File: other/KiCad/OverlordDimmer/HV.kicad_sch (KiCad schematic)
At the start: 23 parts, among them J1 1757310, J2 1757310, Q41 BC817, Q42 2SC4061KT146N, Q43 2SC4061KT146N

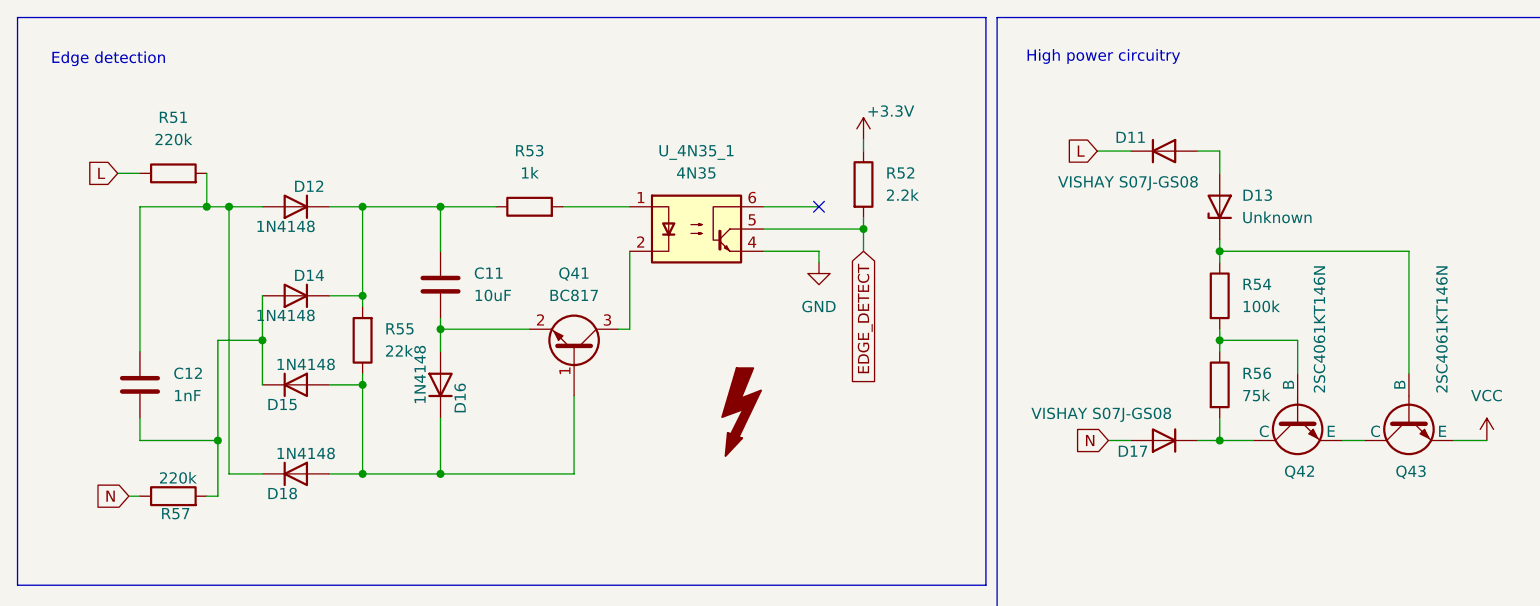
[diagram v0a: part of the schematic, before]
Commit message: sent to production
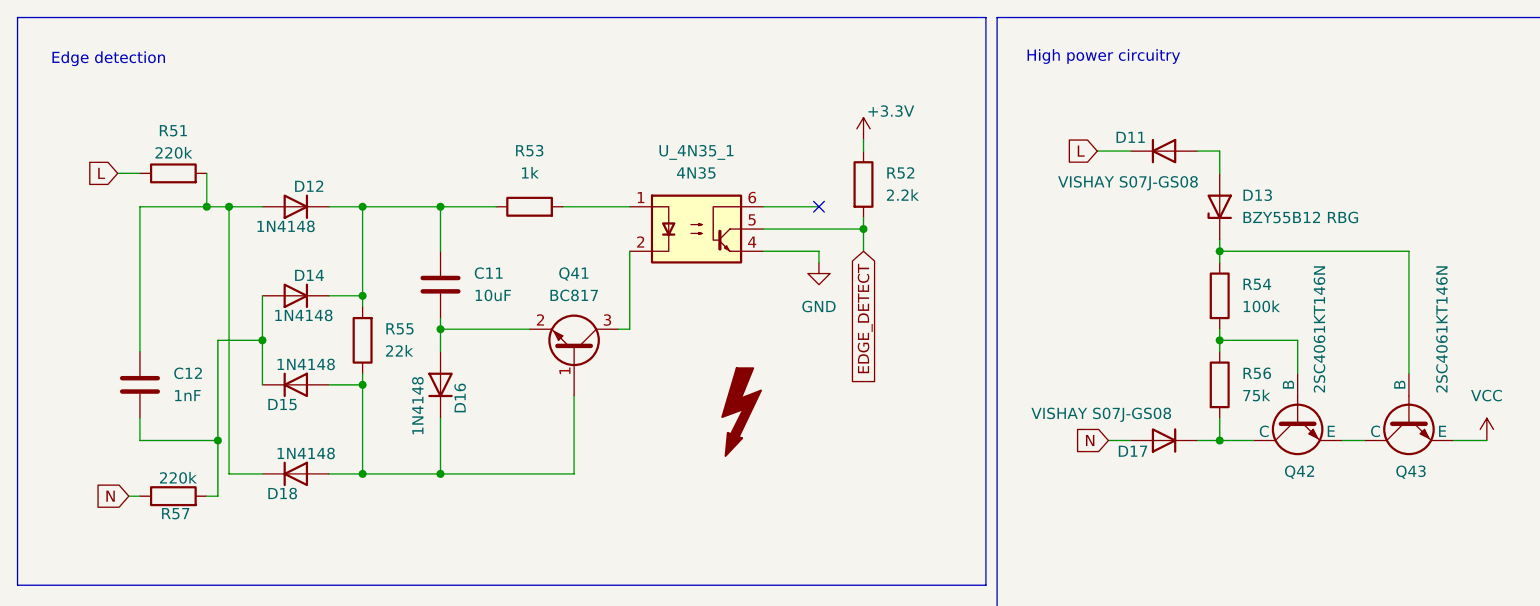
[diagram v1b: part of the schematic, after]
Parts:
- D13: value Unknown -> BZY55B12 RBG
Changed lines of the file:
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@@
-			)
-		)
-		(property "Sim.Enable" ""
-			(at 58.42 55.88 0)
-			(effects
-				(font
-					(size 1.27 1.27)
-				)
-				(hide yes)
 			)
 		)
@@
 			)
 		)
-		(property "Sim.Enable" ""
-			(at 156.21 60.96 0)
-			(effects
-				(font
-					(size 1.27 1.27)
-				)
-				(hide yes)
-			)
-		)
 		(pin "2"
 		)
@@
 			)
 		)
-		(property "Sim.Enable" ""
-			(at 50.8 71.12 0)
-			(effects
-				(font
-					(size 1.27 1.27)
-				)
-				(hide yes)
-			)
-		)
 		(pin "2"
 		)
@@
 		)
 		(property "Sim.Pins" "1=K 2=A"
-			(at 149.86 67.31 0)
-			(effects
-				(font
-					(size 1.27 1.27)
-				)
-				(hide yes)
-			)
-		)
-		(property "Sim.Enable" ""
 			(at 149.86 67.31 0)
 			(effects
@@
 			)
 		)
-		(property "Sim.Enable" ""
-			(at 50.8 60.96 0)
-			(effects
-				(font
-					(size 1.27 1.27)
-				)
-				(hide yes)
-			)
-		)
 		(pin "2"
 		)
@@
 			)
 		)
-		(property "Sim.Enable" ""
-			(at 82.55 57.15 0)
-			(effects
-				(font
-					(size 1.27 1.27)
-				)
-				(hide yes)
-			)
-		)
 		(pin "1"
 		)
@@
 			)
 		)
-		(property "Sim.Enable" ""
-			(at 96.52 43.18 0)
-			(effects
-				(font
-					(size 1.27 1.27)
-				)
-				(hide yes)
-			)
-		)
 		(pin "3"
 		)
@@
 			)
 		)
-		(property "Sim.Enable" ""
-			(at 115.57 38.1 0)
-			(effects
-				(font
-					(size 1.27 1.27)
-				)
-				(hide yes)
-			)
-		)
 		(pin "2"
 		)
@@
 			)
 		)
-		(property "Sim.Enable" ""
-			(at 156.21 50.8 0)
-			(effects
-				(font
-					(size 1.27 1.27)
-				)
-				(hide yes)
-			)
-		)
 		(pin "2"
 		)
@@
 			)
 		)
-		(property "Sim.Enable" ""
-			(at 149.86 34.29 0)
-			(effects
-				(font
-					(size 1.27 1.27)
-				)
-				(hide yes)
-			)
-		)
 		(pin "1"
 		)
@@
 		(on_board yes)
 		(dnp no)
-		(fields_autoplaced yes)
 		(property "Reference" "R51"
-			(at 36.83 30.48 90)
+			(at 36.83 32.004 90)
 			(effects
 				(font
@@
 		)
 		(property "Value" "220k"
-			(at 36.83 33.02 90)
+			(at 36.83 34.544 90)
 			(effects
 				(font
@@
 			)
 		)
-		(property "Sim.Enable" ""
-			(at 36.83 36.83 0)
-			(effects
-				(font
-					(size 1.27 1.27)
-				)
-				(hide yes)
-			)
-		)
 		(pin "1"
 		)
@@
 		)
 		(property "Description" ""
-			(at 36.83 73.66 0)
-			(effects
-				(font
-					(size 1.27 1.27)
-				)
-				(hide yes)
-			)
-		)
-		(property "Sim.Enable" ""
 			(at 36.83 73.66 0)
 			(effects
@@
 			)
 		)
-		(property "Sim.Enable" ""
-			(at 67.31 49.53 0)
-			(effects
-				(font
-					(size 1.27 1.27)
-				)
-				(hide yes)
-			)
-		)
 		(pin "2"
 		)
@@
 			)
 		)
-		(property "Value" "Unknown"
+		(property "Value" "BZY55B12 RBG"
 			(at 158.75 41.9099 90)
 			(effects
@@
 		)
 		(property "Description" "Zener diode"
-			(at 156.21 40.64 0)
-			(effects
-				(font
-					(size 1.27 1.27)
-				)
-				(hide yes)
-			)
-		)
-		(property "Sim.Enable" ""
 			(at 156.21 40.64 0)
 			(effects
@@
 			)
 		)
-		(property "Sim.Enable" ""
-			(at 177.8 64.77 0)
-			(effects
-				(font
-					(size 1.27 1.27)
-				)
-				(hide yes)
-			)
-		)
 		(pin "1"
 		)
@@
 		)
 		(property "Value" "1N4148"
-			(at 65.024 56.388 0)
+			(at 64.77 59.944 0)
 			(effects
 				(font
@@
 			)
 		)
-		(property "Sim.Enable" ""
-			(at 67.31 60.96 0)
-			(effects
-				(font
-					(size 1.27 1.27)
-				)
-				(hide yes)
-			)
-		)
 		(pin "2"
 		)
@@
 		)
 		(property "Sim.Pins" "1=K 2=A"
-			(at 50.8 40.64 0)
-			(effects
-				(font
-					(size 1.27 1.27)
-				)
-				(hide yes)
-			)
-		)
-		(property "Sim.Enable" ""
 			(at 50.8 40.64 0)
 			(effects
@@
 			)
 		)
-		(property "Sim.Enable" ""
-			(at 77.47 40.64 0)
-			(effects
-				(font
-					(size 1.27 1.27)
-				)
-				(hide yes)
-			)
-		)
 		(pin "1"
 		)
@@
 			)
 		)
-		(property "Sim.Enable" ""
-			(at 33.02 60.96 0)
-			(effects
-				(font
-					(size 1.27 1.27)
-				)
-				(hide yes)
-			)
-		)
 		(pin "2"
 		)
@@
 			)
 		)
-		(property "Sim.Enable" ""
-			(at 215.9 71.12 0)
-			(effects
-				(font
-					(size 1.27 1.27)
-				)
-				(hide yes)
-			)
-		)
 		(pin "1"
 		)
@@
 			)
 		)
-		(property "Sim.Enable" ""
-			(at 165.1 64.77 0)
-			(effects
-				(font
-					(size 1.27 1.27)
-				)
-				(hide yes)
-			)
-		)
 		(pin "1"
 		)
@@
 			)
 		)
-		(property "Sim.Enable" ""
-			(at 215.9 36.83 0)
-			(effects
-				(font
-					(size 1.27 1.27)
-				)
-				(hide yes)
-			)
-		)
 		(pin "1"
 		)
@@
 		)
 		(property "Value" "1N4148"
-			(at 46.228 53.086 0)
+			(at 48.26 53.086 0)
 			(effects
 				(font
@@
 			(at 50.8 50.8 0)
 			(effects
-				(font
-					(size 1.27 1.27)
-				)
-				(hide yes)
-			)
-		)
-		(property "Sim.Enable" ""
-			(at 50.8 50.8 0)
-			(effects

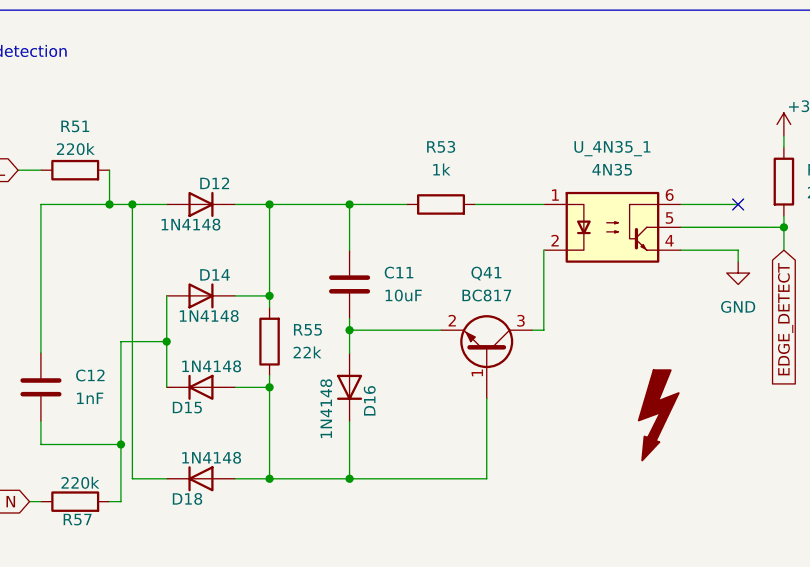
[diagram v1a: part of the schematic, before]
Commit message: update to latest rtdb_gen
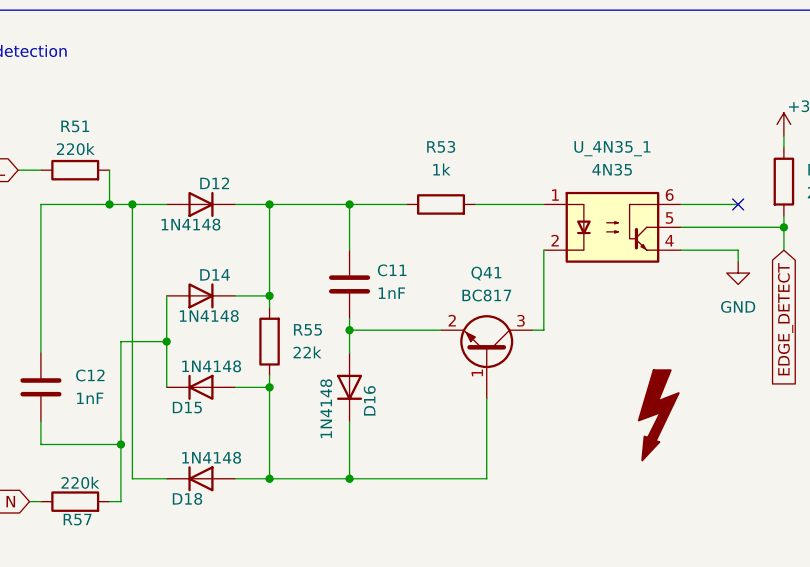
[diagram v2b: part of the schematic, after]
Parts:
- C11: value 10uF -> 1nF
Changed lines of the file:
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@@
 		(on_board yes)
 		(dnp no)
-		(fields_autoplaced yes)
 		(property "Reference" "C11"
-			(at 71.12 48.2599 0)
+			(at 70.358 48.006 0)
 			(effects
 				(font
@@
 			)
 		)
-		(property "Value" "10uF"
-			(at 71.12 50.7999 0)
+		(property "Value" "1nF"
+			(at 70.358 50.546 0)
 			(effects
 				(font

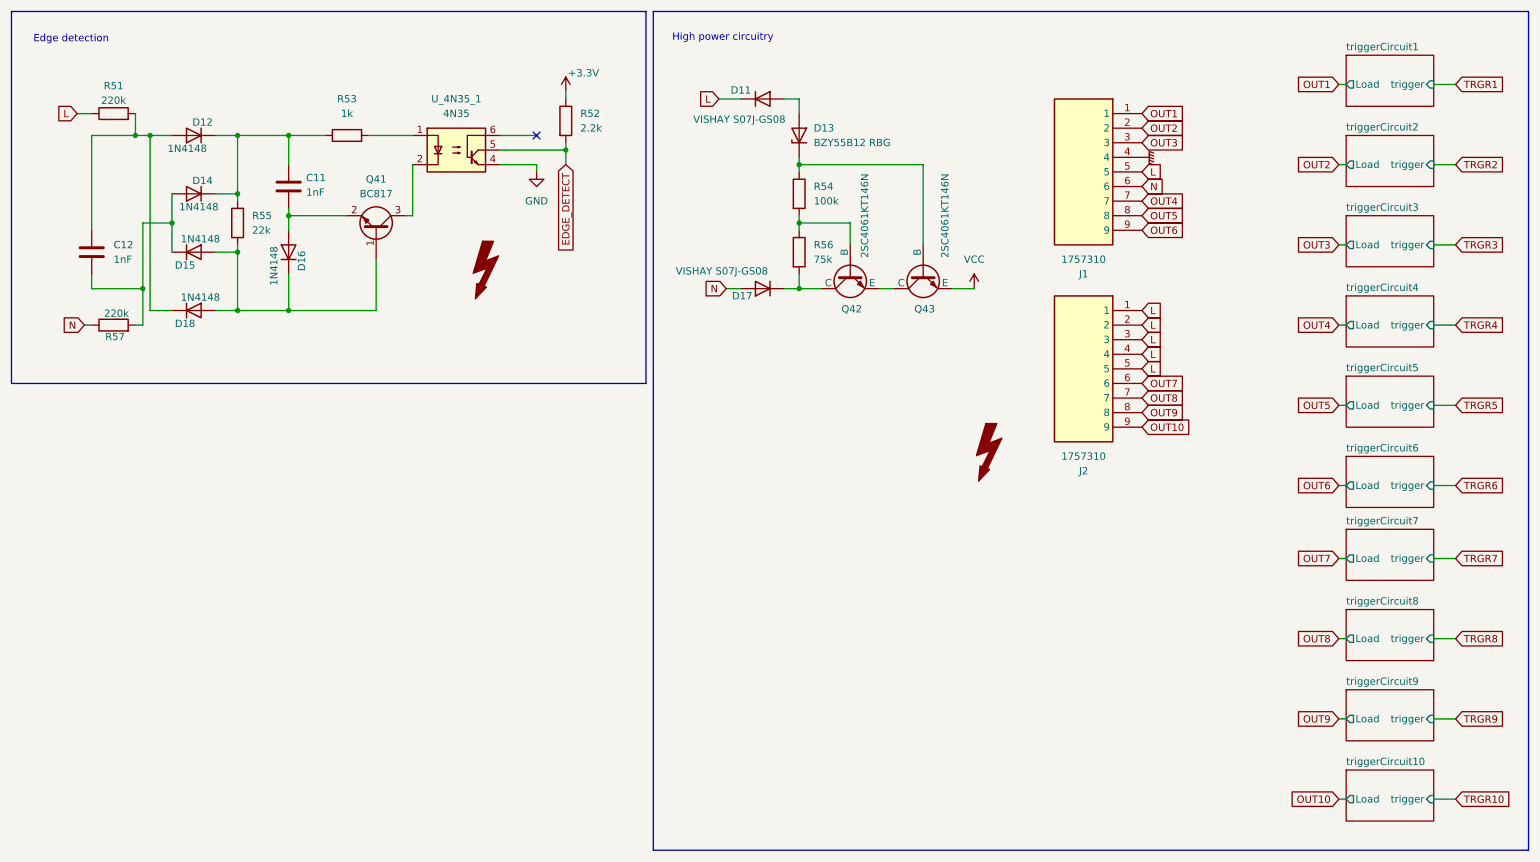
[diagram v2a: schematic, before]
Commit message: Sent for PCB production, ver 1.2 rev A
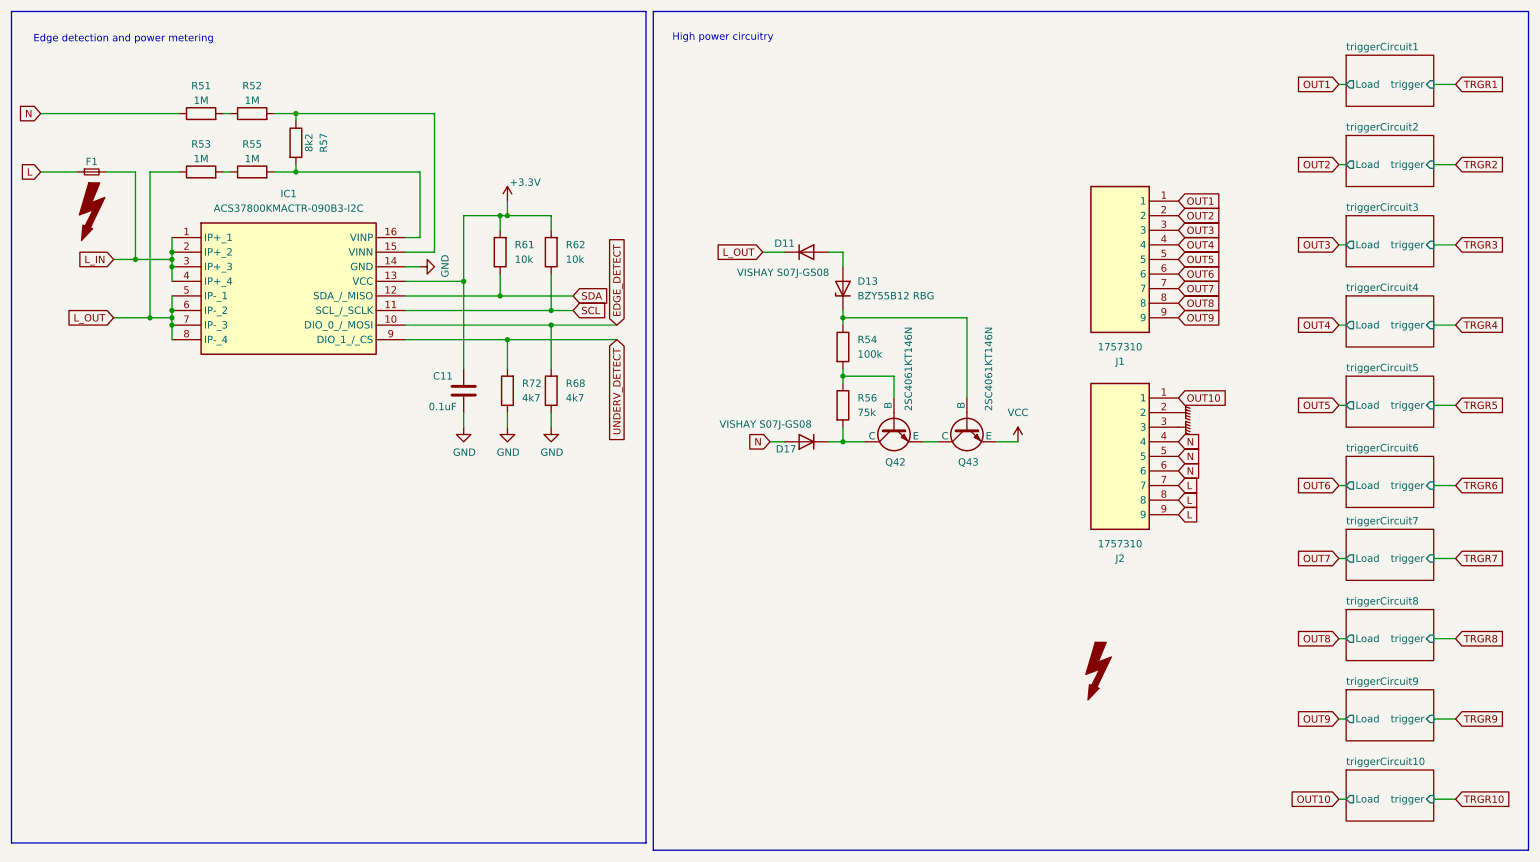
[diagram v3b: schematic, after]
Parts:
- removed C12: 1nF, Capacitor_SMD:C_0805_2012Metric_Pad1.18x1.45mm_HandSolder, symbol Device:C
- removed D12, D14, D15, D16, D18: 1N4148, Diode_SMD:D_0805_2012Metric_Pad1.15x1.40mm_HandSolder, symbol Diode:1N4148
- removed Q41: BC817, Package_TO_SOT_SMD:SOT-23, symbol Transistor_BJT:BC817
- removed U_4N35_1: 4N35, Package_DIP:DIP-6_W7.62mm, symbol Isolator:4N35
- added F1: Fuse_Small, Fuse:Fuseholder_Clip-5x20mm_Bel_FC-203-22_Lateral_P17.80x5.00mm_D1.17mm_Horizontal, symbol Device:Fuse_Small
- added IC1: ACS37800KMACTR-090B3-I2C, SOIC127P1030X265-16N, symbol ACS37800KMACTR-090B3-I2C:ACS37800KMACTR-090B3-I2C
- added R61, R62: 10k, Resistor_SMD:R_0805_2012Metric_Pad1.20x1.40mm_HandSolder, symbol Device:R
- added R68, R72: 4k7, Resistor_SMD:R_0805_2012Metric_Pad1.20x1.40mm_HandSolder, symbol Device:R
- C11: value 1nF -> 0.1uF
- R51: value 220k -> 1M
- R52: value 2.2k -> 1M
- R53: value 1k -> 1M
- R55: value 22k -> 1M
- R57: value 220k -> 8k2
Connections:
- net +3.3V: now also C11.1, IC1.13 (VCC), R61.2, R62.2; no longer R52.1
- net EDGE_DETECT: now also IC1.10 (DIO_0_/_MOSI), R68.2; no longer R52.2
- net GND: now also C11.2, IC1.14 (GND), R68.1, R72.1
- net GNDPWR: now also J2.2, J2.3; no longer J1.4
- net L: now also J2.7, J2.8, J2.9, F1.1; no longer D11.1 (K), J1.5, J2.1, J2.2, J2.3, J2.4, J2.5, R51.1
- net N: now also J2.4, J2.5, J2.6, R51.1; no longer J1.6, R57.1
- net OUT10: now also J2.1; no longer J2.9
- net OUT4: now also J1.4; no longer J1.7
- net OUT5: now also J1.5; no longer J1.8
- net OUT6: now also J1.6; no longer J1.9
- net OUT7: now also J1.7; no longer J2.6
- net OUT8: now also J1.8; no longer J2.7
- net OUT9: now also J1.9; no longer J2.8
- net at R55.1: now also R53.2
- net at R51.2: now also R52.1
- net at R57.2: now also R55.2, IC1.16 (VINP)
- new net: IC1.15 (VINN), R52.2, R57.1
- new net L_IN: F1.2, IC1.1 (IP+_1), IC1.2 (IP+_2), IC1.3 (IP+_3), IC1.4 (IP+_4)
- new net L_OUT: D11.1 (K), IC1.5 (IP-_1), IC1.6 (IP-_2), IC1.7 (IP-_3), IC1.8 (IP-_4), R53.1
- new net SCL: IC1.11 (SCL_/_SCLK), R62.1
- new net SDA: IC1.12 (SDA_/_MISO), R61.1
- new net UNDERV_DETECT: IC1.9 (DIO_1_/_CS), R72.2
- no-connect marks 1 -> 0
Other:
- note added: "Edge detection and power metering"
- note removed: "Edge detection"
- moved on the sheet: D11, D13, D17, J1, J2, Q42, Q43, R51, R54, R56

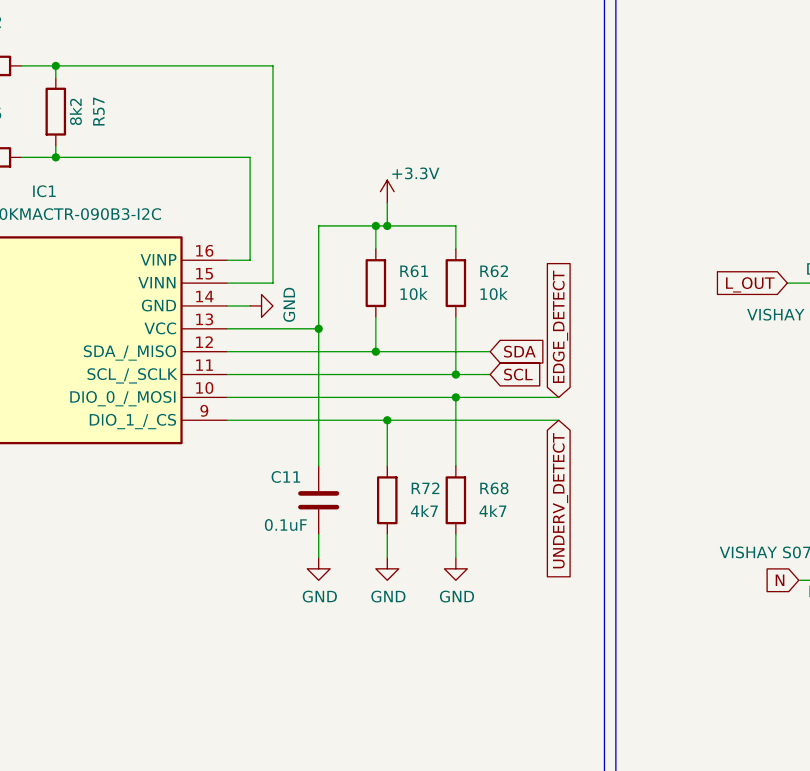
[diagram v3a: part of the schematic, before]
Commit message: Updated PCB design - added pullup on boot pin GPIO0 - schematic cleanup - removed unused power supply parts
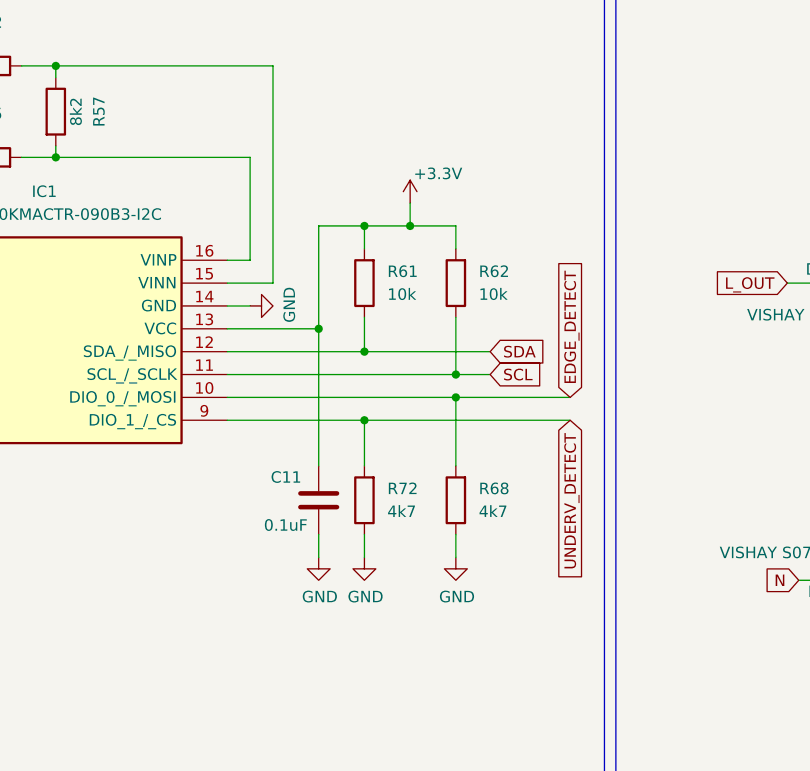
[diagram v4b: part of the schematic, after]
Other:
- moved on the sheet: R61, R72
